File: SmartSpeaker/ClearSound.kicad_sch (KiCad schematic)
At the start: 29 parts

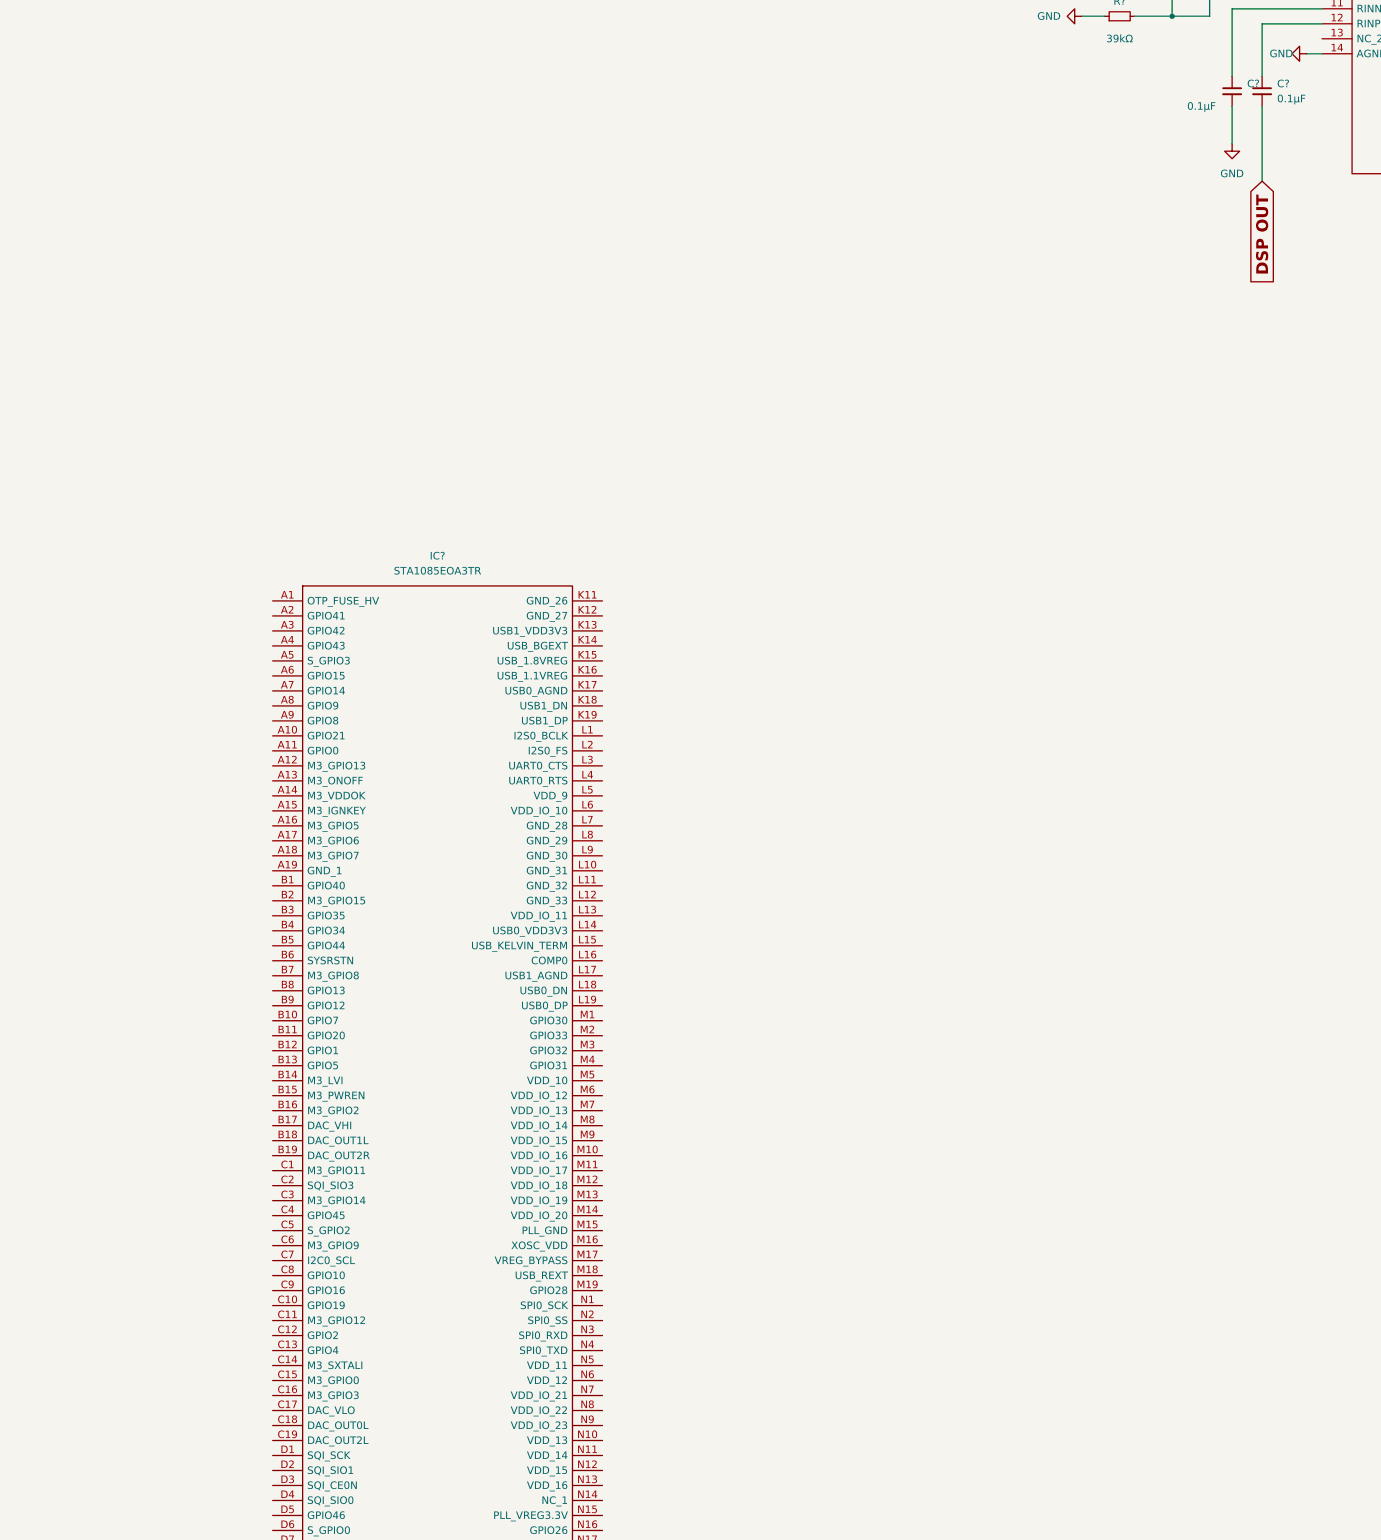
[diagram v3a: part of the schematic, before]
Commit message: connected amp to DSP
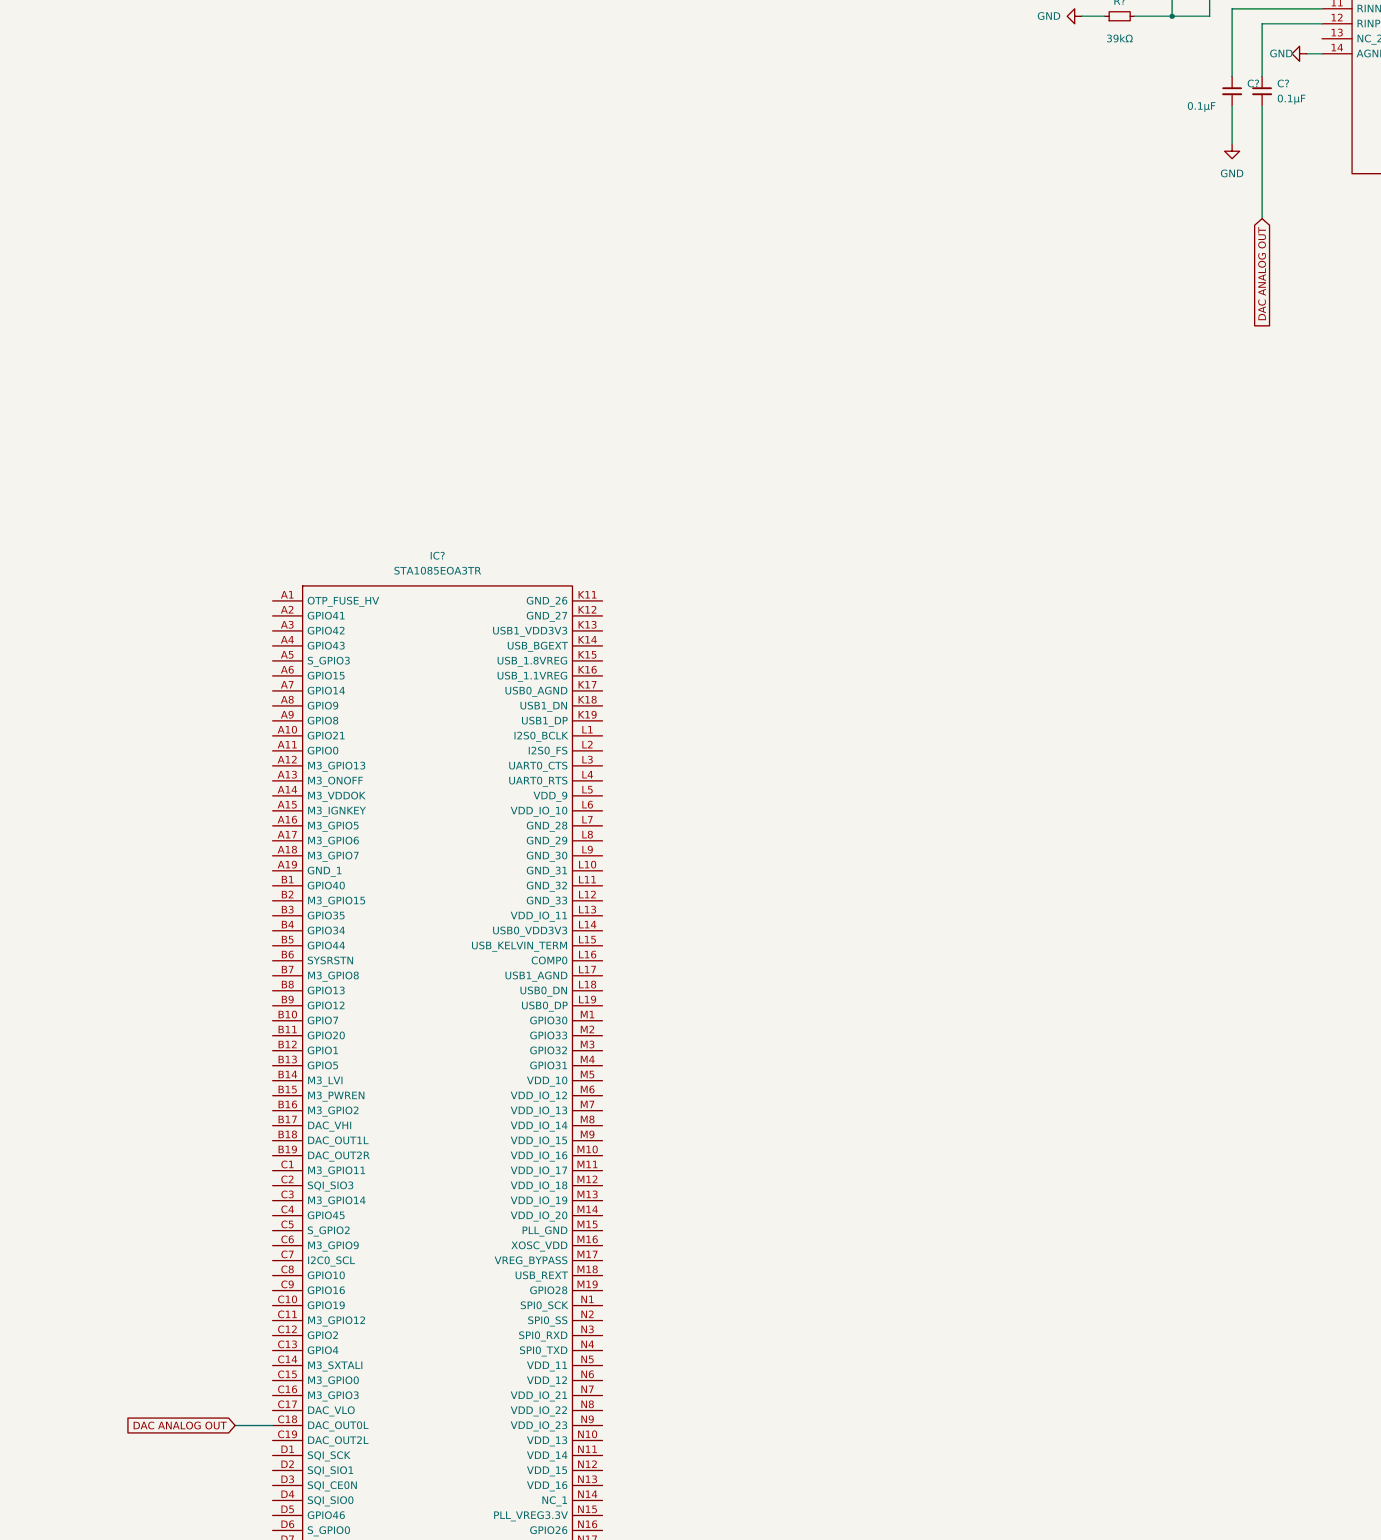
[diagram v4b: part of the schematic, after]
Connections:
- net DSP OUT is gone; now on net DAC ANALOG OUT: C?.2
- net DAC ANALOG OUT: now reaches IC?.C18 (DAC_OUT0L)
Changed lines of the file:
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@@
+    (stroke (width 0) (type default) (color 0 0 0 0))
+  )
+  (wire (pts (xy 436.88 92.71) (xy 436.88 111.76))
     (stroke (width 0) (type default) (color 0 0 0 0))
   )
@@
     (stroke (width 0) (type default) (color 0 0 0 0))
   )
-  (wire (pts (xy 436.88 92.71) (xy 436.88 105.41))
-    (stroke (width 0) (type default) (color 0 0 0 0))
-  )
   (wire (pts (xy 431.8 57.15) (xy 414.02 57.15))
     (stroke (width 0) (type default) (color 0 0 0 0))
@@
   )
   (wire (pts (xy 55.88 637.54) (xy 68.58 637.54))
+    (stroke (width 0) (type default) (color 0 0 0 0))
+  )
+  (wire (pts (xy 262.89 316.23) (xy 269.24 316.23))
     (stroke (width 0) (type default) (color 0 0 0 0))
   )
@@
     )
   )
+  (global_label "DAC ANALOG OUT" (shape input) (at 262.89 316.23 180) (fields_autoplaced)
+    (effects (font (size 1.27 1.27)) (justify right))
+    (property "Intersheet References" "${INTERSHEET_REFS}" (id 0) (at 244.1483 316.1506 0)
+      (effects (font (size 1.27 1.27)) (justify right) hide)
+    )
+  )
   (global_label "ANTENNA" (shape input) (at 54.61 640.08 180) (fields_autoplaced)
     (effects (font (size 1.27 1.27)) (justify right))
     (property "Intersheet References" "${INTERSHEET_REFS}" (id 0) (at 43.9117 640.0006 0)
+      (effects (font (size 1.27 1.27)) (justify right) hide)
+    )
+  )
+  (global_label "DAC ANALOG OUT" (shape input) (at 436.88 111.76 270) (fields_autoplaced)
+    (effects (font (size 1.27 1.27)) (justify right))
+    (property "Intersheet References" "${INTERSHEET_REFS}" (id 0) (at 436.8006 130.5017 90)
       (effects (font (size 1.27 1.27)) (justify right) hide)
     )
@@
     )
   )
-  (global_label "DSP OUT" (shape input) (at 436.88 105.41 270) (fields_autoplaced)
-    (effects (font (size 2 2) (thickness 0.4) bold) (justify right))
-    (property "Intersheet References" "${INTERSHEET_REFS}" (id 0) (at 436.68 122.6529 90)
-      (effects (font (size 2 2) (thickness 0.4) bold) (justify right) hide)
-    )
-  )

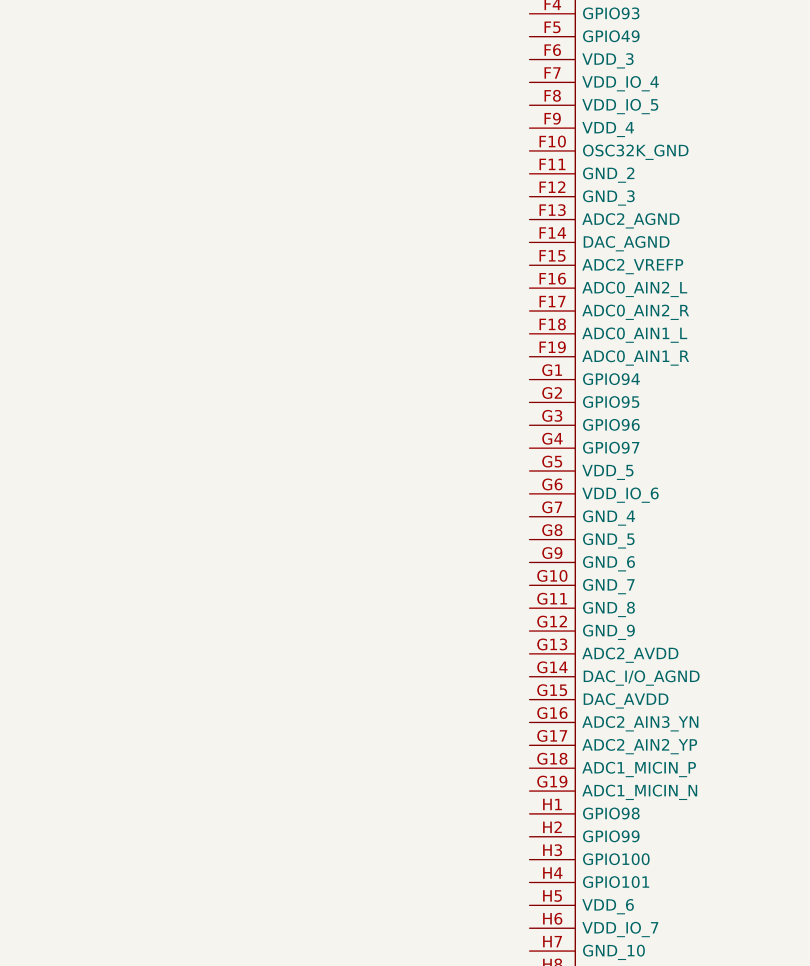
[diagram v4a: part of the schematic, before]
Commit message: Add GND/stuff to DSP
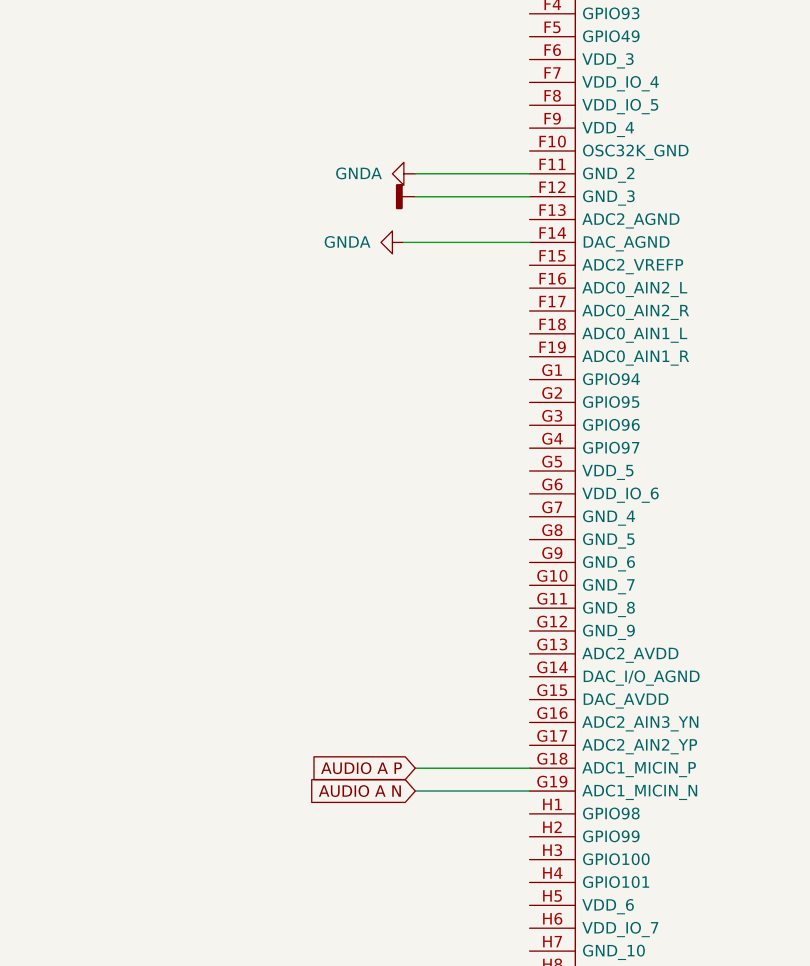
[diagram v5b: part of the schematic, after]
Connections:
- net GNDD: now also IC?.F12 (GND_3)
- net GNDA: now reaches IC?.F11 (GND_2)
- net GNDA: now also IC?.F14 (DAC_AGND)
- net AUDIO A P: now reaches IC?.G18 (ADC1_MICIN_P)
- net AUDIO A N: now reaches IC?.G19 (ADC1_MICIN_N)
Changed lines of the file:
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@@
+    (stroke (width 0) (type default) (color 0 0 0 0))
+  )
+  (wire (pts (xy 256.54 443.23) (xy 269.24 443.23))
     (stroke (width 0) (type default) (color 0 0 0 0))
   )
@@
     (stroke (width 0) (type default) (color 0 0 0 0))
   )
+  (wire (pts (xy 256.54 511.81) (xy 269.24 511.81))
+    (stroke (width 0) (type default) (color 0 0 0 0))
+  )
   (wire (pts (xy 55.88 627.38) (xy 68.58 627.38))
     (stroke (width 0) (type default) (color 0 0 0 0))
@@
     (stroke (width 0) (type default) (color 0 0 0 0))
   )
+  (wire (pts (xy 256.54 509.27) (xy 269.24 509.27))
+    (stroke (width 0) (type default) (color 0 0 0 0))
+  )
   (wire (pts (xy 491.49 134.62) (xy 491.49 139.7))
     (stroke (width 0) (type default) (color 0 0 0 0))
@@
     (stroke (width 0) (type default) (color 0 0 0 0))
   )
+  (wire (pts (xy 255.27 450.85) (xy 269.24 450.85))
+    (stroke (width 0) (type default) (color 0 0 0 0))
+  )
   (wire (pts (xy 511.81 55.88) (xy 511.81 58.42))
     (stroke (width 0) (type default) (color 0 0 0 0))
@@
   )
   (wire (pts (xy 262.89 316.23) (xy 269.24 316.23))
+    (stroke (width 0) (type default) (color 0 0 0 0))
+  )
+  (wire (pts (xy 256.54 445.77) (xy 269.24 445.77))
     (stroke (width 0) (type default) (color 0 0 0 0))
   )
@@
     (property "Intersheet References" "${INTERSHEET_REFS}" (id 0) (at 515.1302 134.5406 0)
       (effects (font (size 1.27 1.27)) (justify left) hide)
+    )
+  )
+  (global_label "AUDIO A P" (shape input) (at 256.54 509.27 180) (fields_autoplaced)
+    (effects (font (size 1.27 1.27)) (justify right))
+    (property "Intersheet References" "${INTERSHEET_REFS}" (id 0) (at 244.2088 509.1906 0)
+      (effects (font (size 1.27 1.27)) (justify right) hide)
     )
   )
@@
     )
   )
+  (global_label "AUDIO A N" (shape input) (at 256.54 511.81 180) (fields_autoplaced)
+    (effects (font (size 1.27 1.27)) (justify right))
+    (property "Intersheet References" "${INTERSHEET_REFS}" (id 0) (at 244.1483 511.7306 0)
+      (effects (font (size 1.27 1.27)) (justify right) hide)
+    )
+  )
   (global_label "SHUTDOWN" (shape input) (at 439.42 44.45 90) (fields_autoplaced)
     (effects (font (size 1.27 1.27)) (justify left))
@@
     (pin "1")
     (pin "2")
+  )
+  (symbol (lib_id "power:GNDA") (at 256.54 443.23 270) (unit 1)
+    (in_bom yes) (on_board yes)
+    (property "Reference" "#PWR?" (id 0) (at 250.19 443.23 0)
+      (effects (font (size 1.27 1.27)) hide)
+    )
+    (property "Value" "GNDA" (id 1) (at 247.65 443.23 90)
+      (effects (font (size 1.27 1.27)) (justify left))
+    )
+    (property "Footprint" "" (id 2) (at 256.54 443.23 0)
+      (effects (font (size 1.27 1.27)) hide)
+    )
+    (property "Datasheet" "" (id 3) (at 256.54 443.23 0)
+      (effects (font (size 1.27 1.27)) hide)
+    )
+    (pin "1")
   )
   (symbol (lib_id "AMP:TPA3138D2PWPR") (at 447.04 50.8 0) (unit 1)
@@
     (pin "2")
   )
+  (symbol (lib_id "power:GNDA") (at 255.27 450.85 270) (unit 1)
+    (in_bom yes) (on_board yes)
+    (property "Reference" "#PWR?" (id 0) (at 248.92 450.85 0)
+      (effects (font (size 1.27 1.27)) hide)
+    )
+    (property "Value" "GNDA" (id 1) (at 246.38 450.85 90)
+      (effects (font (size 1.27 1.27)) (justify left))
+    )
+    (property "Footprint" "" (id 2) (at 255.27 450.85 0)
+      (effects (font (size 1.27 1.27)) hide)
+    )
+    (property "Datasheet" "" (id 3) (at 255.27 450.85 0)
+      (effects (font (size 1.27 1.27)) hide)
+    )
+    (pin "1")
+  )
   (symbol (lib_id "Device:R_Small") (at 430.53 53.34 90) (unit 1)
     (in_bom yes) (on_board yes)
@@
     )
     (property "Datasheet" "" (id 3) (at 523.24 104.14 0)
+      (effects (font (size 1.27 1.27)) hide)
+    )
+    (pin "1")
+  )
+  (symbol (lib_id "power:GNDD") (at 256.54 445.77 270) (unit 1)
+    (in_bom yes) (on_board yes) (fields_autoplaced)
+    (property "Reference" "#PWR?" (id 0) (at 250.19 445.77 0)
+      (effects (font (size 1.27 1.27)) hide)
+    )
+    (property "Value" "" (id 1) (at 252.73 445.7699 90)
+      (effects (font (size 1.27 1.27)) (justify right))
+    )
+    (property "Footprint" "" (id 2) (at 256.54 445.77 0)
+      (effects (font (size 1.27 1.27)) hide)
+    )
+    (property "Datasheet" "" (id 3) (at 256.54 445.77 0)
       (effects (font (size 1.27 1.27)) hide)
     )
@@
   )
   (symbol_instances
+    (path "/0b58772f-4203-4c46-822d-4fa6602f722f"
+      (reference "#PWR?") (unit 1) (value "GNDA") (footprint "")
+    )
     (path "/14f0b4d0-8aea-4d44-acd6-4d675abff585"
       (reference "#PWR?") (unit 1) (value "VDD") (footprint "")
@@
       (reference "#PWR?") (unit 1) (value "GND") (footprint "")
     )
+    (path "/2cf6a90c-d963-4fc1-9dfd-28f5547e5ba5"
+      (reference "#PWR?") (unit 1) (value "GNDA") (footprint "")
+    )
     (path "/3b809d5e-1cd6-4bd7-8775-d6e8648b017c"
       (reference "#PWR?") (unit 1) (value "GND") (footprint "")
@@
       (reference "#PWR?") (unit 1) (value "VDD") (footprint "")
     )
+    (path "/78e0a86d-ac34-4bc6-8007-e394bc3b92fd"
+      (reference "#PWR?") (unit 1) (value "GNDD") (footprint "")
+    )
     (path "/8134730b-a903-4315-bd4f-88a61ea90ef6"

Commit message: second amp
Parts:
- added C? (x2): 0.47µF, symbol Device:C_Small
- added C? (x2): 0.68µF, symbol Device:C_Small
- added C? (x2): 100µF, symbol Device:C_Polarized_Small_US
- added C? (x2): 1000pF, symbol Device:C_Small
- added C? (x5): 0.1µF, symbol Device:C_Small
- added C?: 1µF, symbol Device:C_Small
- added IC?: TPA3138D2PWPR, SOP65P640X120-29N, symbol AMP:TPA3138D2PWPR
- added L? (x2): 10µH, symbol Device:L_Iron
- added R? (x3): 100kΩ, symbol Device:R_Small
- added R?: 39kΩ, symbol Device:R_Small
- added R?: 51k Ω, symbol Device:R_Small
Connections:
- net GND: now also J?.2 (Pin_2), J?.2 (Pin_2), C?.1, C?.2, C?.2, C?.2, C?.2, C?.2, C?.2, C?.2, C?.2, C?.2, C?.2, IC?.14 (AGND), IC?.19 (GND_2), IC?.24 (GND_3), IC?.29 (THERMAL_PAD), IC?.3 (LINP), IC?.4 (LINN), IC?.8 (GND_1), R?.1
- net SHUTDOWN: now also IC?.2 (~{SD}/~{FAULT}), R?.2
- net VDD: now also C?.1, C?.1, C?.1, C?.1, C?.1, C?.1, C?.1, IC?.15 (PVCCR_1), IC?.16 (PVCCR_2), IC?.27 (PVCCL_1), IC?.28 (PVCCL_2), IC?.7 (AVCC), R?.1, R?.1, R?.1
- net at J?.1 (Pin_1): now also J?.1 (Pin_1), C?.2
- new net: C?.1, IC?.17 (BSPR), IC?.21 (BSNR)
- new net: C?.2, IC?.18 (OUTPR), IC?.20 (OUTNR), L?.1
- new net: C?.1, L?.2 (x2)
- new net: IC?.5 (GAIN_SEL), R?.2
- new net: IC?.10 (PLIMIT), R?.1, R?.2
- new net: C?.1, IC?.11 (RINN)
- new net: C?.1, IC?.12 (RINP)
- new net: C?.1, IC?.22 (BSNL), IC?.26 (BSPL)
- new net: C?.2, IC?.23 (OUTNL), IC?.25 (OUTPL), L?.1
- new net: IC?.6 (MODE_SEL), R?.2
- new net: C?.2, IC?.9 (GVDD), R?.2
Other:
- moved on the sheet: J?
